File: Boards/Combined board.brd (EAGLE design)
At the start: 60.9 x 84.8 mm, 6 parts

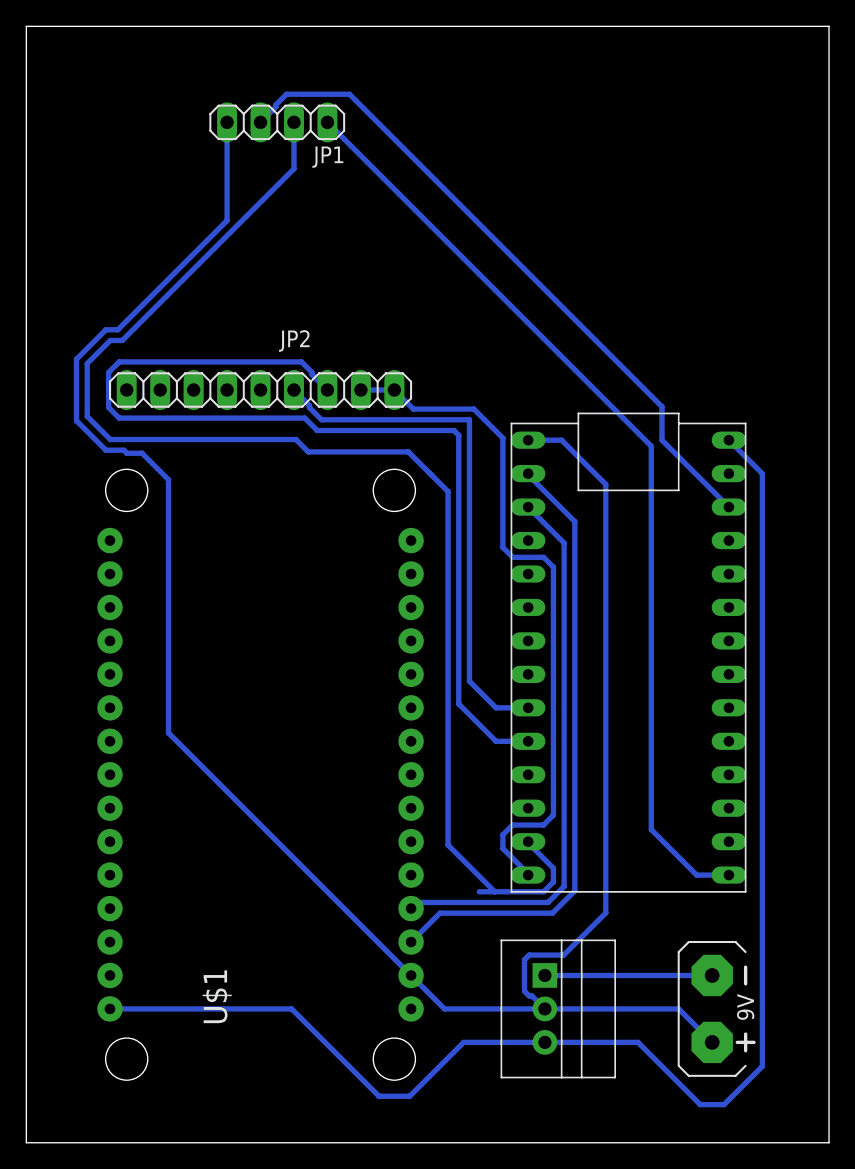
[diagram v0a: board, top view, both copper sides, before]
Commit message: Board can't be printed
:(
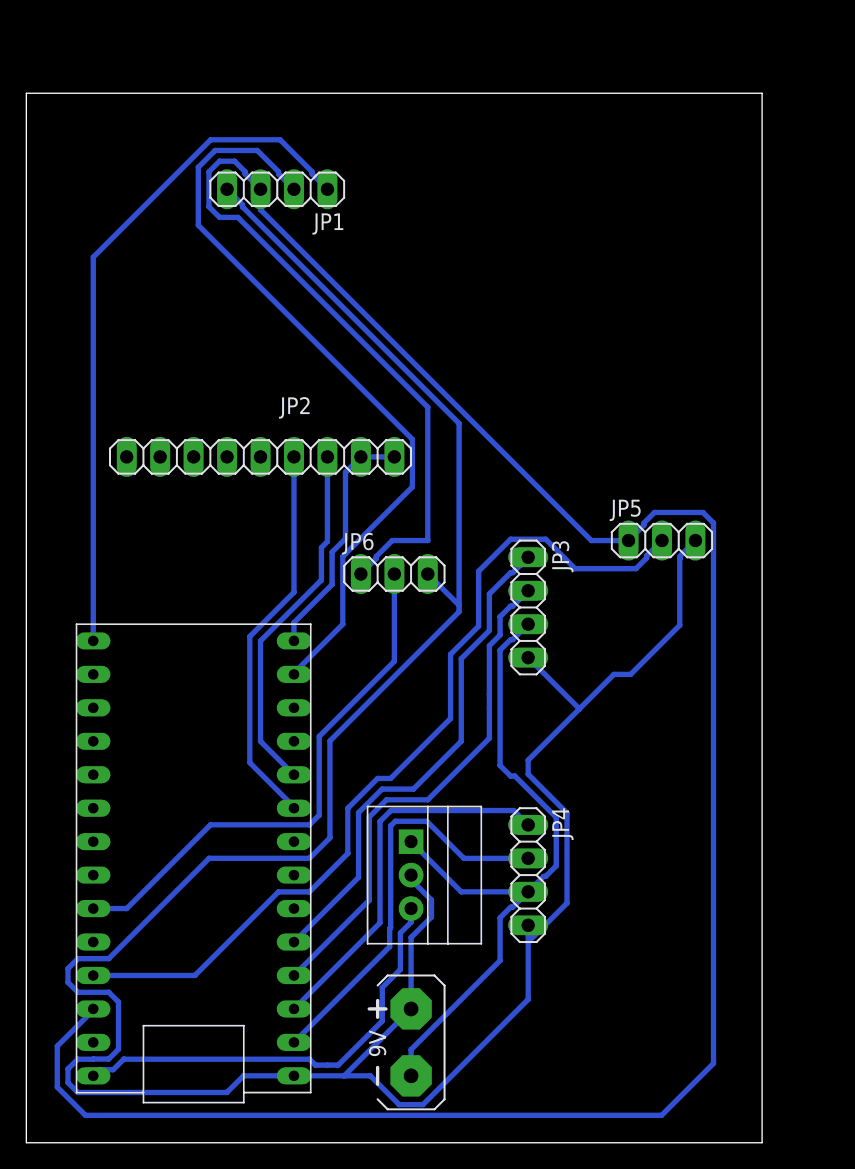
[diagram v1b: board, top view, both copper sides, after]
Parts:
- removed U$1: ESP12E_DEVKIT, ESP12E_DEVKIT:ESP12E_DEVKIT
- added JP3, JP4: (no value), HyTechDevices:1X04
- added JP5, JP6: (no value), HyTechDevices:1X03
- moved U$2 25.4 mm to (47.0, 39.4), turned to 180 degrees
- moved G1 23.0 mm to (54.6, 7.62), turned to 0 degrees
- moved U$3 14.4 mm to (54.6, 20.3)
- moved JP1 5.08 mm to (44.5, 72.4)
- moved JP2 5.08 mm to (44.5, 52.1)
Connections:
- removed net N$11: U$1.RX, U$2.D1(TX1)
- removed net N$4: U$1.TX, U$2.D0(RX1)
- new net MOT1_1: JP3.2, U$2.D2
- new net MOT1_2: JP3.1, U$2.D3(CANTX)
- new net MOT2_1: JP4.2, U$2.D0(RX1)
- new net MOT2_2: JP4.1, U$2.D1(TX1)
- new net POT1: JP5.2, U$2.A9
- new net POT2: JP6.2, U$2.A7
- net 3.3V: now also JP5.1, JP6.1
- net 5V: no longer U$1.VIN
- net 9V: now also JP3.3, JP4.3
- net GND: now also JP3.4, JP4.4, JP5.3, JP6.3; no longer U$1.GND@3
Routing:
- net 3.3V: track 51.0 -> 195.2 mm
- net 5V: track 105.7 -> 33.5 mm
- net POT1: track 0.00 -> 66.1 mm
- net GND: track 159.0 -> 211.2 mm
- net CSAG: track 74.9 -> 27.3 mm
- net N$4: track 47.2 -> 0.00 mm
- net SDA: track 100.8 -> 58.1 mm
- net N$11: track 42.2 -> 0.00 mm
- net POT2: track 0.00 -> 40.8 mm
- net 9V: track 12.7 -> 52.4 mm
- net MOT1_1: track 0.00 -> 38.5 mm
- net MOT1_2: track 0.00 -> 38.1 mm
- net SDD: track 52.2 -> 18.6 mm
- net MOT2_1: track 0.00 -> 31.2 mm
- net MOT2_2: track 0.00 -> 29.0 mm
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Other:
- board size 60.9 x 84.8 mm -> 55.9 x 79.7 mm

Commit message: Final Push
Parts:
- added R1: 1kohm, HyTechDevices:AXIAL-0.3
- added RESET_BUTTON: (no value), HyTechDevices:B3F-10XX
- renumbered JP2 to IMU, JP3 to MOT1_CONTROLLER, JP4 to MOT2_CONTROLLER, JP5 to POT1, JP6 to POT2, U$3 to 5V_REGULATOR
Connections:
- new net N$1: R1.P$1, RESET_BUTTON.4, U$2.A2
- net 3.3V: now also RESET_BUTTON.1
- net GND: now also R1.P$2; no longer U$2.GND
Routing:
- net GND: track 211.2 -> 308.5 mm
- net N$1: track 0.00 -> 80.7 mm
- net 3.3V: track 195.2 -> 217.7 mm
